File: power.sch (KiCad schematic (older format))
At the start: 17 parts, among them U11 5M1270ZT144C5N, U18 MIC5356-SGYMME

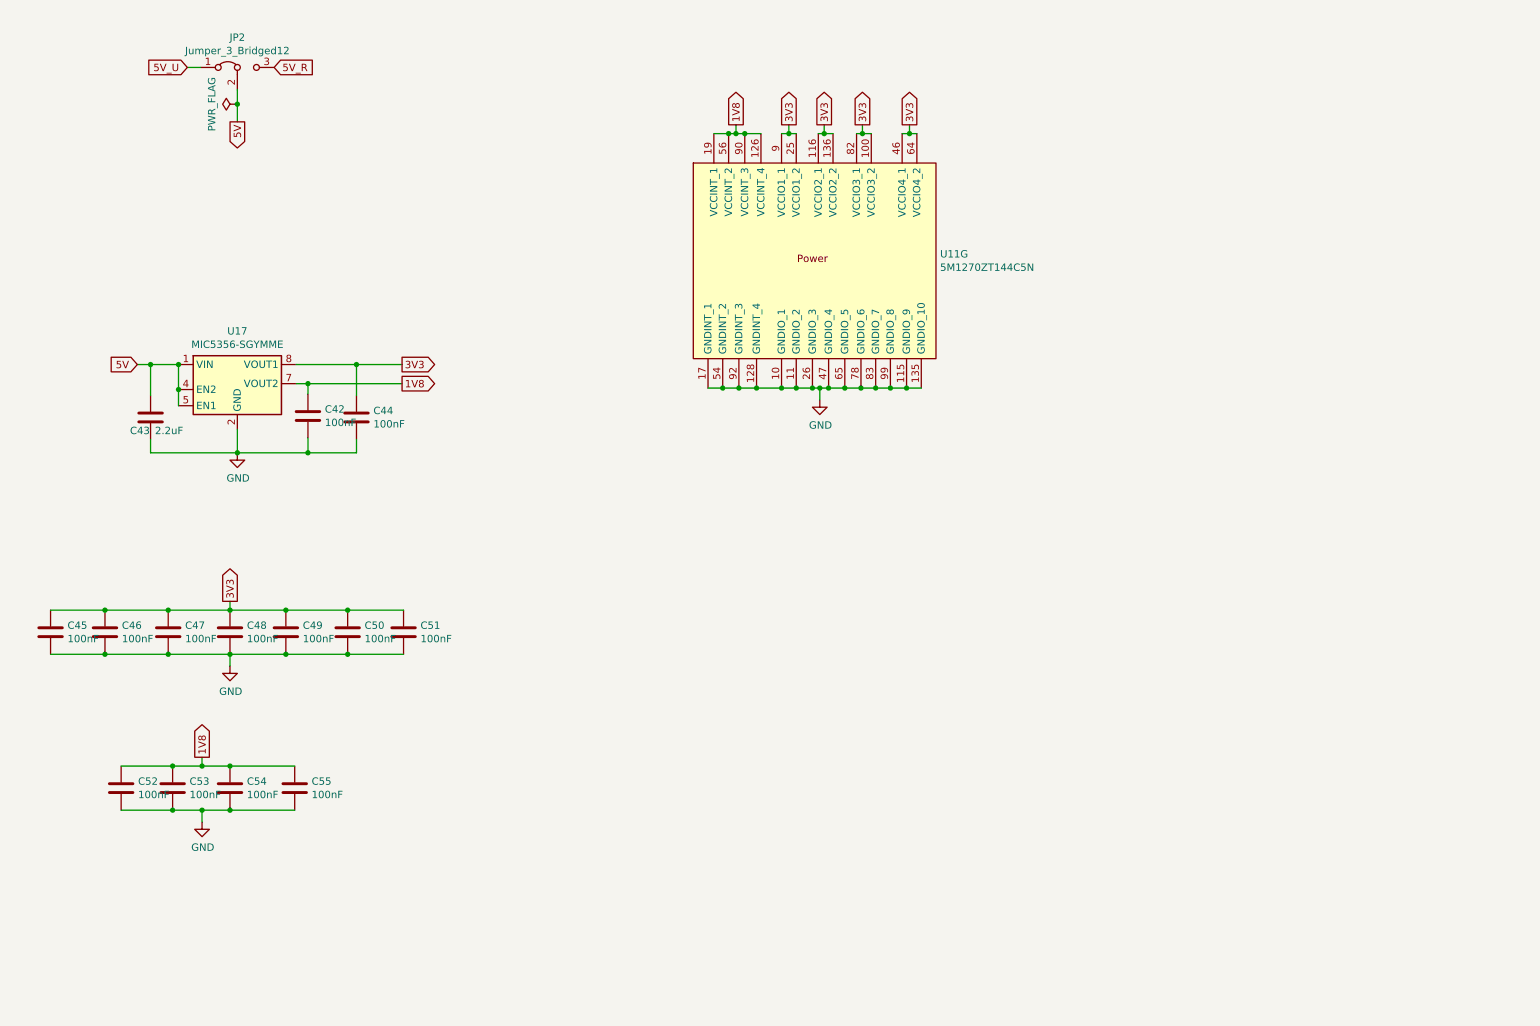
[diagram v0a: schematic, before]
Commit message: recovered layout
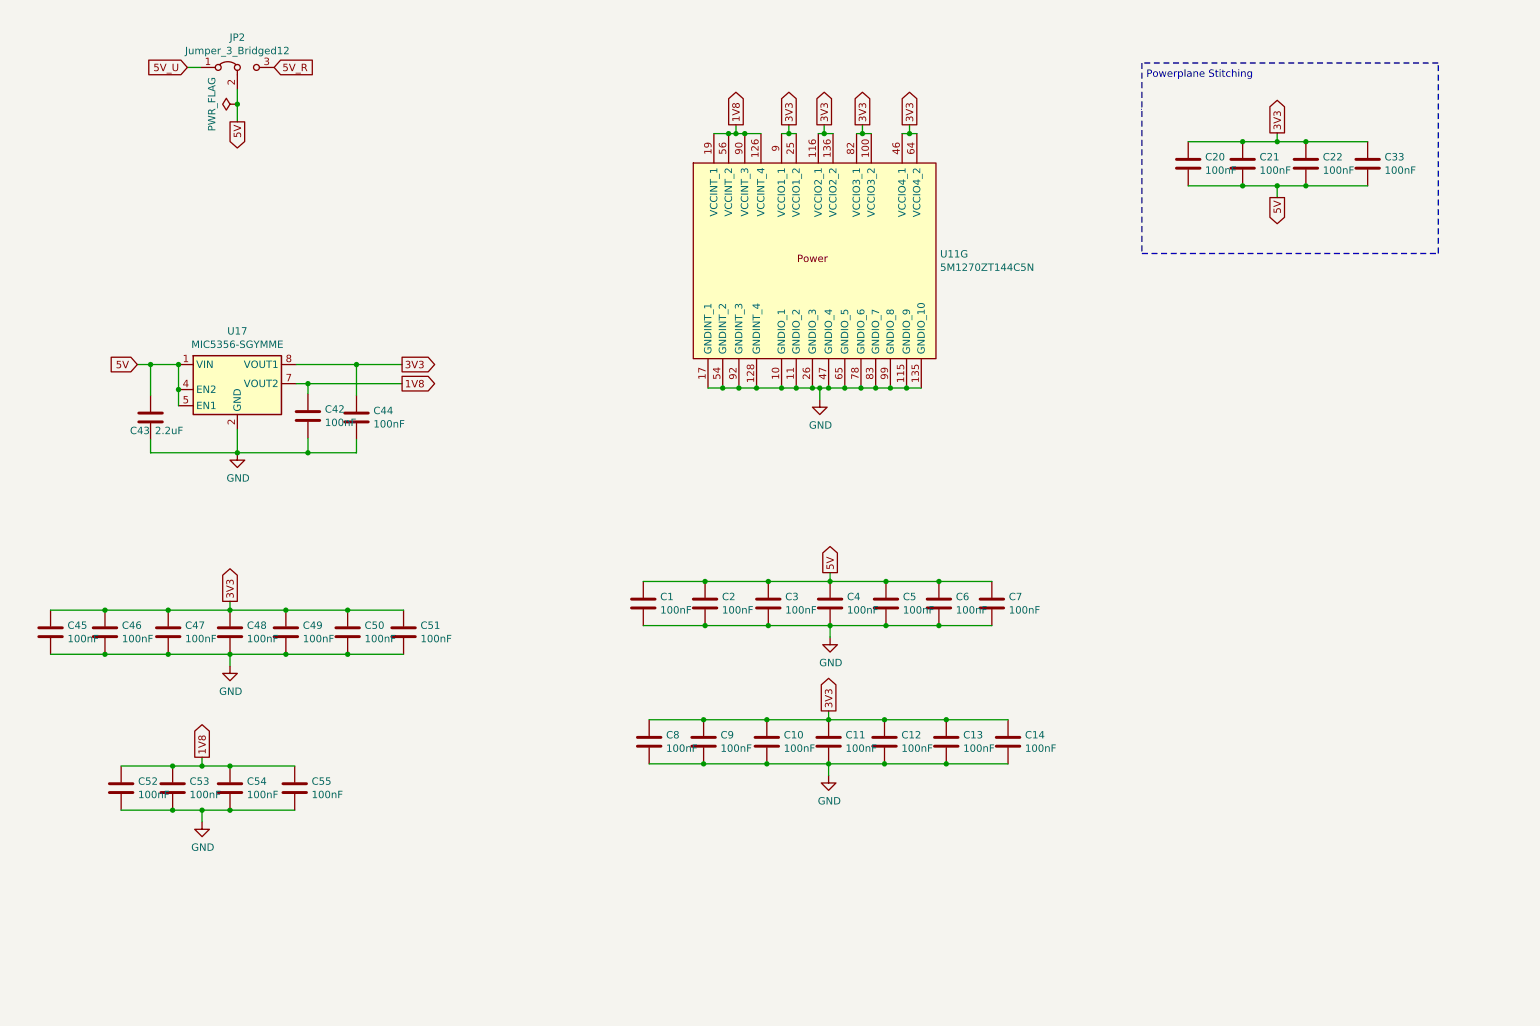
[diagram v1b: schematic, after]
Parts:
- added C1, C10, C11, C12, C13, C14, C2, C3, C4, C5, C6, C7, C8, C9: 100nF, Capacitor_SMD:C_0603_1608Metric_Pad1.05x0.95mm_HandSolder, symbol Device:C
- added C20, C21, C22, C33: 100nF, Capacitor_SMD:C_0805_2012Metric_Pad1.15x1.40mm_HandSolder, symbol Device:C
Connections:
- net 3V3: now also C10.1, C11.1, C12.1, C13.1, C14.1, C20.1, C21.1, C22.1, C33.1, C8.1, C9.1
- net 5V: now also C1.1, C2.1, C20.2, C21.2, C22.2, C3.1, C33.2, C4.1, C5.1, C6.1, C7.1
- net GND: now also C1.2, C10.2, C11.2, C12.2, C13.2, C14.2, C2.2, C3.2, C4.2, C5.2, C6.2, C7.2, C8.2, C9.2
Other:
- note added: "Powerplane Stitching"

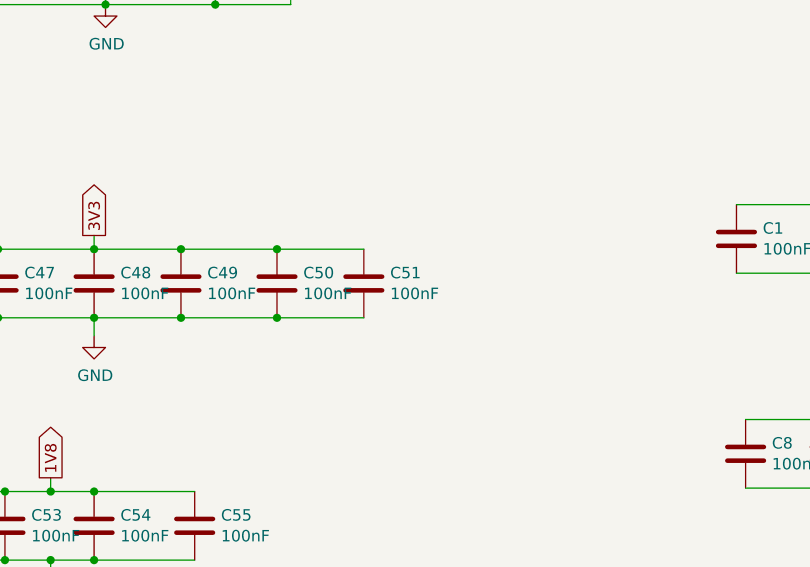
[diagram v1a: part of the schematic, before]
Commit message: placed all parts
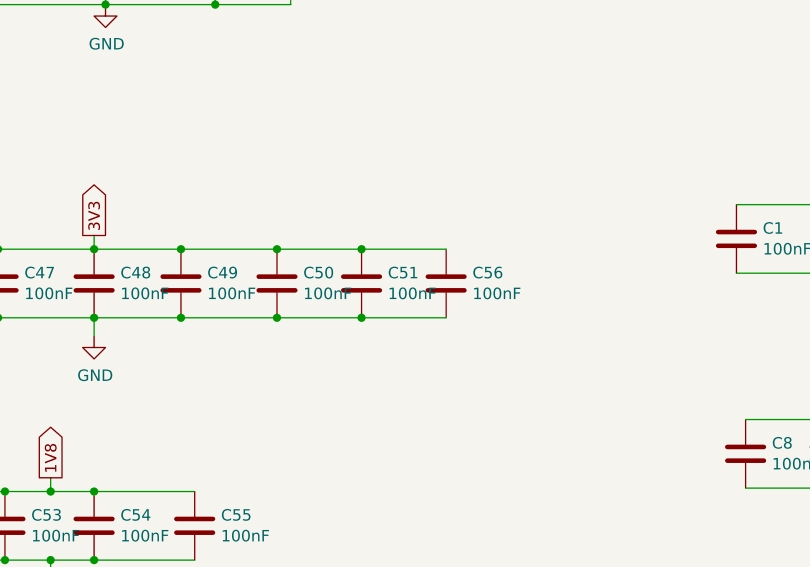
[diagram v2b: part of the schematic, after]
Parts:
- added C56: 100nF, Capacitor_SMD:C_0603_1608Metric_Pad1.05x0.95mm_HandSolder, symbol Device:C
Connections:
- net 3V3: now also C56.1
- net GND: now also C56.2
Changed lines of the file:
@@
 L Device:C C?
 U 1 1 5D3E1517
-P 3270 5130
+P 3260 5130
 AR Path="/5CFABACD/5D3E1517" Ref="C?"  Part="1"
 AR Path="/5D3E1517" Ref="C?"  Part="1"
 AR Path="/5D2A5E4A/5D3E1517" Ref="C51"  Part="1"
 AR Path="/5CFABACD/5D2103A8/5D3E1517" Ref="C51"  Part="1"
-F 0 "C51" H 3385 5176 50  0000 L CNN
-F 1 "100nF" H 3385 5085 50  0000 L CNN
-F 2 "Capacitor_SMD:C_0603_1608Metric_Pad1.05x0.95mm_HandSolder" H 3308 4980 50  0001 C CNN
-F 3 "https://www.mouser.com/datasheet/2/396/mlcc02_e-1307760.pdf" H 3270 5130 50  0001 C CNN
-F 4 "Multilayer Ceramic Capacitors MLCC - SMD/SMT 0.1uF 25V X5R +/-10% 0603 Gen Purp" H 3385 5276 50  0001 C CNN "Description"
-F 5 "Taiyo Yuden" H -2030 -1570 50  0001 C CNN "MFR"
-F 6 "TMK107BJ104KA-T" H -2030 -1570 50  0001 C CNN "MPN"
-F 7 "963-TMK107BJ104KA-T" H 3385 5276 50  0001 C CNN "SPN"
-F 8 "Mouser" H -2030 -1570 50  0001 C CNN "SPR"
-F 9 "https://www.mouser.com/ProductDetail/963-TMK107BJ104KA-T" H -2030 -1570 50  0001 C CNN "SPURL"
-	1    3270 5130
+F 0 "C51" H 3375 5176 50  0000 L CNN
+F 1 "100nF" H 3375 5085 50  0000 L CNN
+F 2 "Capacitor_SMD:C_0603_1608Metric_Pad1.05x0.95mm_HandSolder" H 3298 4980 50  0001 C CNN
+F 3 "https://www.mouser.com/datasheet/2/396/mlcc02_e-1307760.pdf" H 3260 5130 50  0001 C CNN
+F 4 "Multilayer Ceramic Capacitors MLCC - SMD/SMT 0.1uF 25V X5R +/-10% 0603 Gen Purp" H 3375 5276 50  0001 C CNN "Description"
+F 5 "Taiyo Yuden" H -2040 -1570 50  0001 C CNN "MFR"
+F 6 "TMK107BJ104KA-T" H -2040 -1570 50  0001 C CNN "MPN"
+F 7 "963-TMK107BJ104KA-T" H 3375 5276 50  0001 C CNN "SPN"
+F 8 "Mouser" H -2040 -1570 50  0001 C CNN "SPR"
+F 9 "https://www.mouser.com/ProductDetail/963-TMK107BJ104KA-T" H -2040 -1570 50  0001 C CNN "SPURL"
+	1    3260 5130
 	1    0    0    -1
 $EndComp
@@
 Wire Wire Line
 	1350 6340 1700 6340
-Wire Wire Line
-	3270 5280 2890 5280
-Wire Wire Line
-	3270 4980 2890 4980
 Wire Wire Line
 	1670 5280 2090 5280
@@
 Text Notes 8320 1370 0    50   ~ 0
 Powerplane Stitching
+$Comp
+L Device:C C?
+U 1 1 5D1048B7
+P 3630 5130
+AR Path="/5CFABACD/5D1048B7" Ref="C?"  Part="1"
+AR Path="/5D1048B7" Ref="C?"  Part="1"
+AR Path="/5D2A5E4A/5D1048B7" Ref="C?"  Part="1"
+AR Path="/5CFABACD/5D2103A8/5D1048B7" Ref="C56"  Part="1"
+F 0 "C56" H 3745 5176 50  0000 L CNN
+F 1 "100nF" H 3745 5085 50  0000 L CNN
+F 2 "Capacitor_SMD:C_0603_1608Metric_Pad1.05x0.95mm_HandSolder" H 3668 4980 50  0001 C CNN
+F 3 "https://www.mouser.com/datasheet/2/396/mlcc02_e-1307760.pdf" H 3630 5130 50  0001 C CNN
+F 4 "Multilayer Ceramic Capacitors MLCC - SMD/SMT 0.1uF 25V X5R +/-10% 0603 Gen Purp" H 3745 5276 50  0001 C CNN "Description"
+F 5 "Taiyo Yuden" H -1670 -1570 50  0001 C CNN "MFR"
+F 6 "TMK107BJ104KA-T" H -1670 -1570 50  0001 C CNN "MPN"
+F 7 "963-TMK107BJ104KA-T" H 3745 5276 50  0001 C CNN "SPN"
+F 8 "Mouser" H -1670 -1570 50  0001 C CNN "SPR"
+F 9 "https://www.mouser.com/ProductDetail/963-TMK107BJ104KA-T" H -1670 -1570 50  0001 C CNN "SPURL"
+	1    3630 5130
+	1    0    0    -1
+$EndComp
+Wire Wire Line
+	2890 5280 3260 5280
+Wire Wire Line
+	2890 4980 3260 4980
+Connection ~ 3260 4980
+Wire Wire Line
+	3260 4980 3630 4980
+Connection ~ 3260 5280
+Wire Wire Line
+	3260 5280 3630 5280
 $EndSCHEMATC

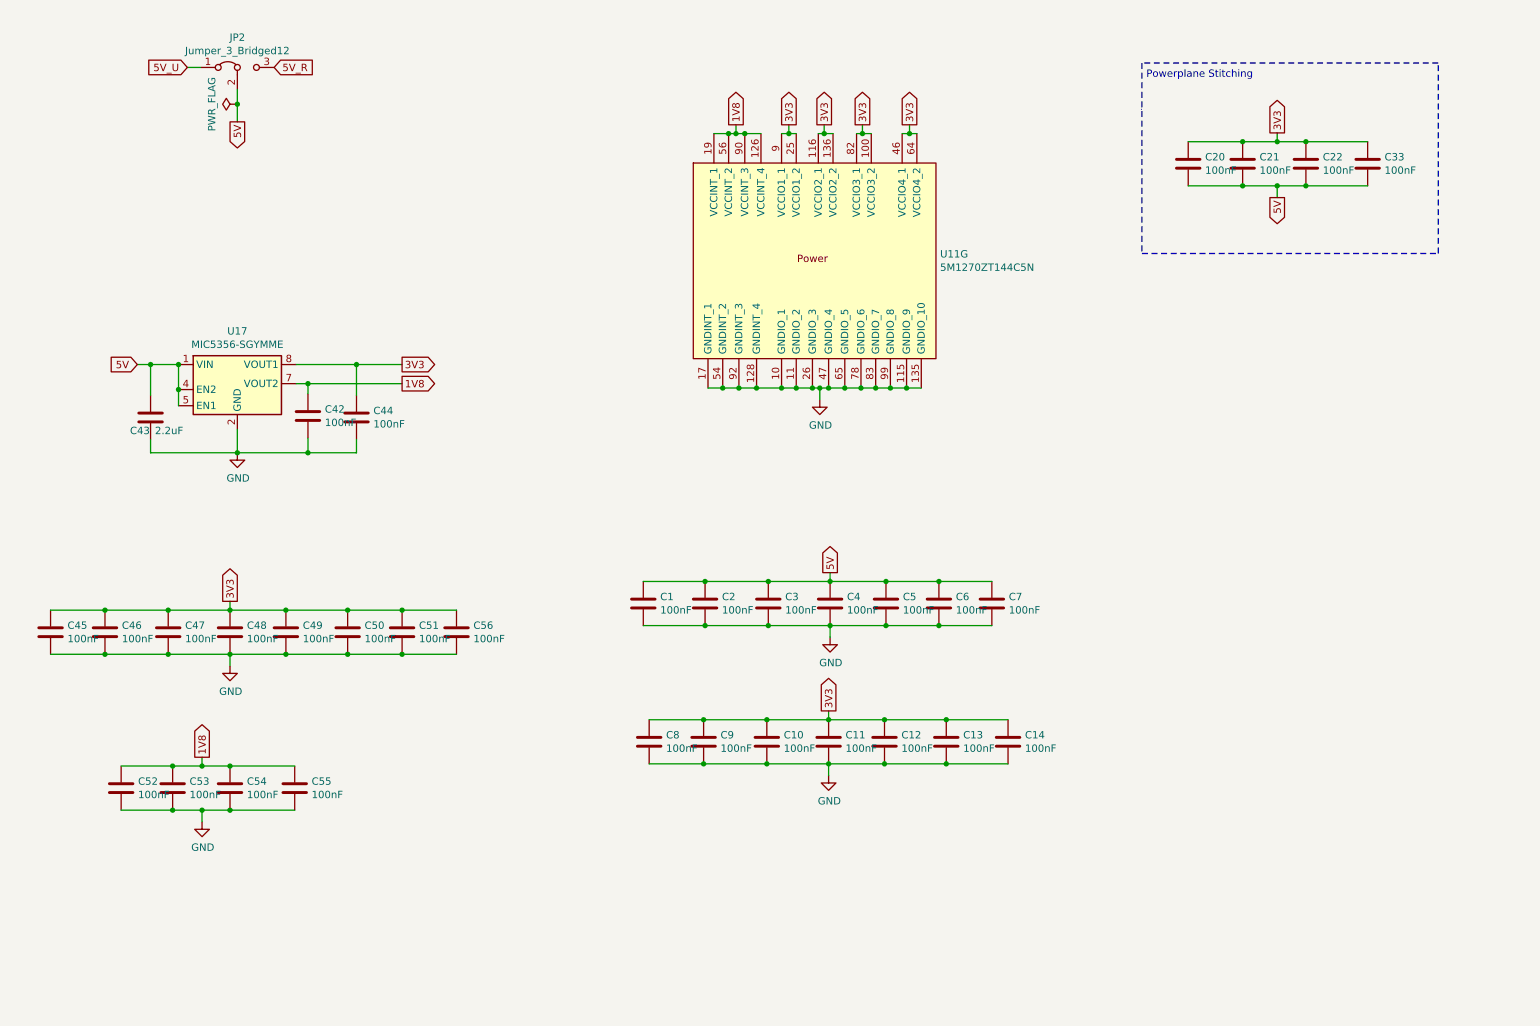
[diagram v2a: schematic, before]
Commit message: Added bus structure, additional pins added, 5V load balancer
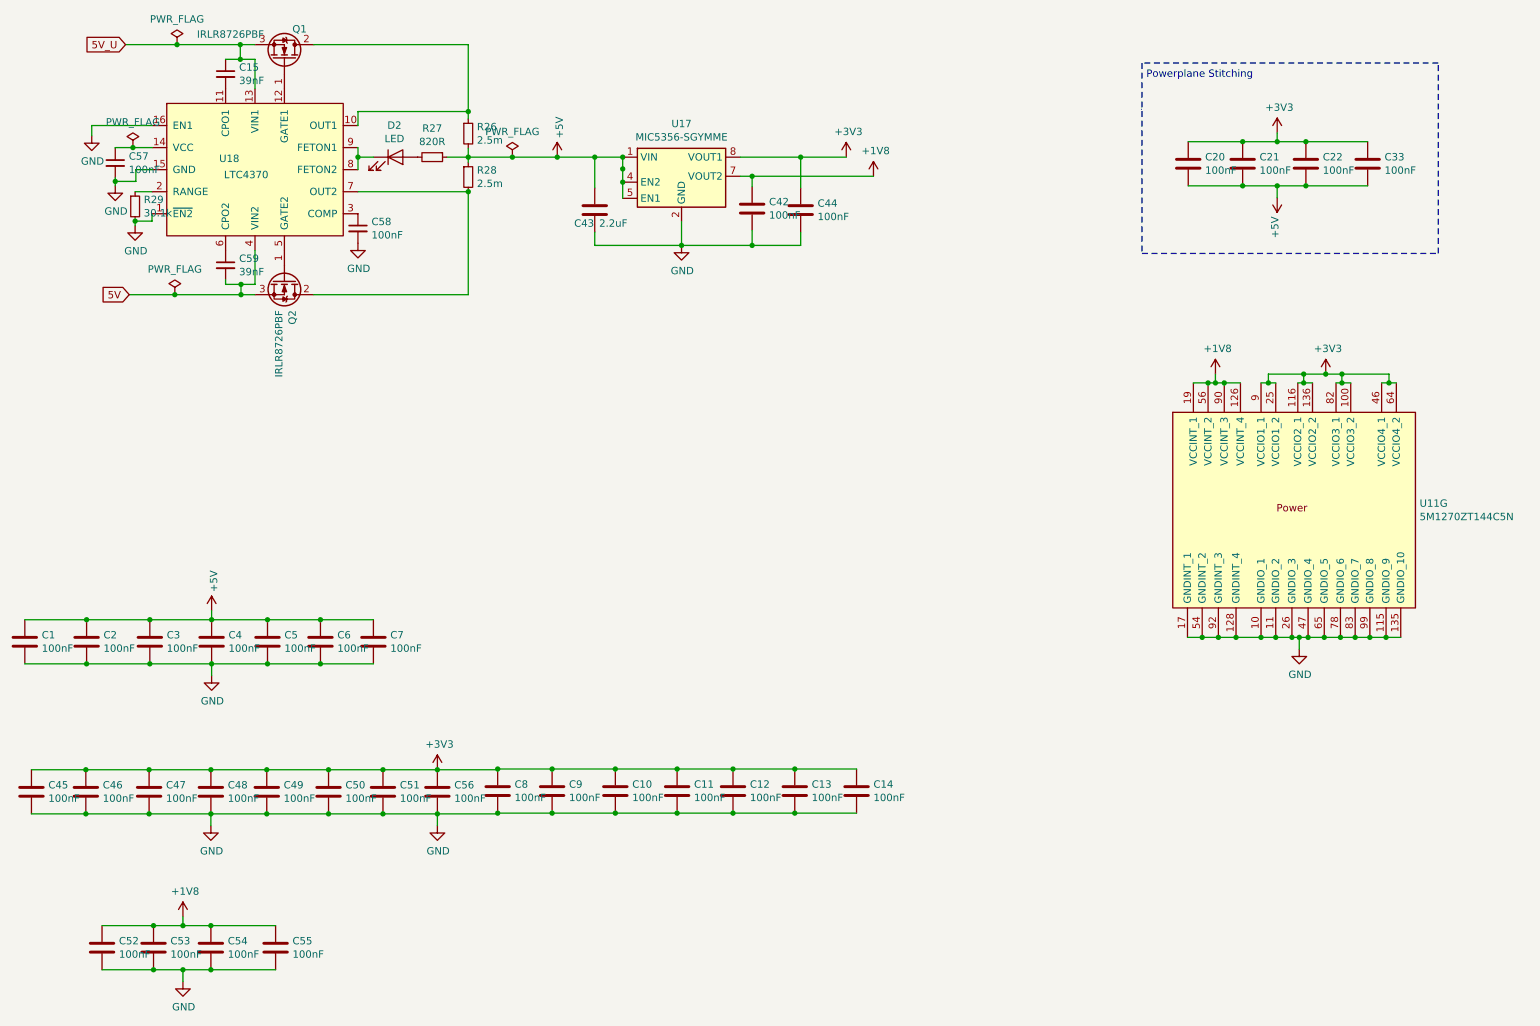
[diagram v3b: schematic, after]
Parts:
- removed JP2: Jumper_3_Bridged12, Connector_PinHeader_2.54mm:PinHeader_1x03_P2.54mm_Vertical, symbol Jumper:Jumper_3_Bridged12
- added C15, C59: 39nF, Capacitor_SMD:C_0603_1608Metric_Pad1.05x0.95mm_HandSolder, symbol Device:C_Small
- added C57, C58: 100nF, Capacitor_SMD:C_0603_1608Metric_Pad1.05x0.95mm_HandSolder, symbol Device:C_Small
- added D2: LED, LED_SMD:LED_0603_1608Metric_Pad1.05x0.95mm_HandSolder, symbol Device:LED
- added Q1, Q2: IRLR8726PBF, Package_TO_SOT_SMD:TO-252-3_TabPin4, symbol power_share-rescue:IRLR8726PBF-Transistor_FET
- added R26, R28: 2.5m, Resistor_SMD:R_2512_6332Metric_Pad1.52x3.35mm_HandSolder, symbol Device:R_Small
- added R27: 820R, Resistor_SMD:R_0603_1608Metric_Pad1.05x0.95mm_HandSolder, symbol Device:R_Small
- added R29: 30.1k, Resistor_SMD:R_0603_1608Metric_Pad1.05x0.95mm_HandSolder, symbol Device:R_Small
- added U18: LTC4370, Package_SO:MSOP-16_3x4.039mm_P0.5mm, symbol power_share-rescue:LTC4370-Power_Management
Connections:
- net 5V: now also C59.2, Q2.3 (S), U18.4 (VIN2); no longer C1.1, C2.1, C20.2, C21.2, C22.2, C3.1, C33.2, C4.1, C43.1, C5.1, C6.1, C7.1, U18.1 (VIN), U18.4 (EN2), U18.5 (EN1)
- net 5V_U: now also C15.1, Q1.3 (S), U18.13 (VIN1)
- net GND: now also C57.2, C58.2, R29.2, U18.1 (~EN2), U18.15 (GND), U18.16 (EN1)
- net +5V: now reaches U18.3 (NC)
- net +5V: now also C1.1, C2.1, C20.2, C21.2, C22.2, C3.1, C33.2, C4.1, C43.1, C5.1, C6.1, C7.1, U18.1 (VIN), U18.4 (EN2), U18.5 (EN1), R26.2, R27.1, R28.1
- net 1V8 renamed +1V8
- net 3V3 renamed +3V3
- new net: Q1.2 (D), Q1.4 (D), R26.1, U18.10 (OUT1)
- new net: C15.2, U18.11 (CPO1)
- new net: Q1.1 (G), U18.12 (GATE1)
- new net: C57.1, U18.14 (VCC)
- new net: R29.1, U18.2 (RANGE)
- new net: C58.1, U18.3 (COMP)
- new net: Q2.1 (G), U18.5 (GATE2)
- new net: C59.1, U18.6 (CPO2)
- new net: Q2.2 (D), Q2.4 (D), R28.2, U18.7 (OUT2)
- new net: D2.1 (K), U18.8 (FETON2), U18.9 (FETON1)
- new net: D2.2 (A), R27.2
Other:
- moved on the sheet: C1, C10, C11, C12, C13, C14, C2, C3, C4, C42, C43, C44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

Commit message: updated rescue
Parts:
- Q1, Q2: symbol power_share-rescue:IRLR8726PBF-Transistor_FET -> rc2014_max_v-rescue:IRLR8726PBF-Transistor_FET-power_share-rescue
- U18: symbol power_share-rescue:LTC4370-Power_Management -> rc2014_max_v-rescue:LTC4370-Power_Management-power_share-rescue
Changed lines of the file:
@@
 	1730 1135 2160 1135
 $Comp
-L power_share-rescue:IRLR8726PBF-Transistor_FET Q2
+L rc2014_max_v-rescue:IRLR8726PBF-Transistor_FET-power_share-rescue Q2
 U 1 1 5D16AE64
 P 2460 2735
+AR Path="/5D16AE64" Ref="Q2"  Part="1"
+AR Path="/5CFABACD/5D2103A8/5D16AE64" Ref="Q2"  Part="1"
 F 0 "Q2" H 2666 2789 50  0000 L CNN
 F 1 "IRLR8726PBF" H 2666 2698 50  0000 L CNN
@@
 $EndComp
 $Comp
-L power_share-rescue:IRLR8726PBF-Transistor_FET Q1
+L rc2014_max_v-rescue:IRLR8726PBF-Transistor_FET-power_share-rescue Q1
 U 1 1 5D1697F4
 P 2460 1235
+AR Path="/5D1697F4" Ref="Q1"  Part="1"
+AR Path="/5CFABACD/5D2103A8/5D1697F4" Ref="Q1"  Part="1"
 F 0 "Q1" V 2666 1289 50  0000 L CNN
 F 1 "IRLR8726PBF" V 2630 640 50  0000 L CNN
@@
 Connection ~ 2960 1900
 $Comp
-L power_share-rescue:LTC4370-Power_Management U18
+L rc2014_max_v-rescue:LTC4370-Power_Management-power_share-rescue U18
 U 1 1 5D15CEC4
 P 2260 1985
